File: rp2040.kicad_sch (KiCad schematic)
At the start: 27 parts, among them J3 Conn_01x02, J4 USB_B_Micro, U4 NCP1117-3.3_SOT223, U5 W25Q128JVS, U6 RP2040, Y2 ABM8-272-T3

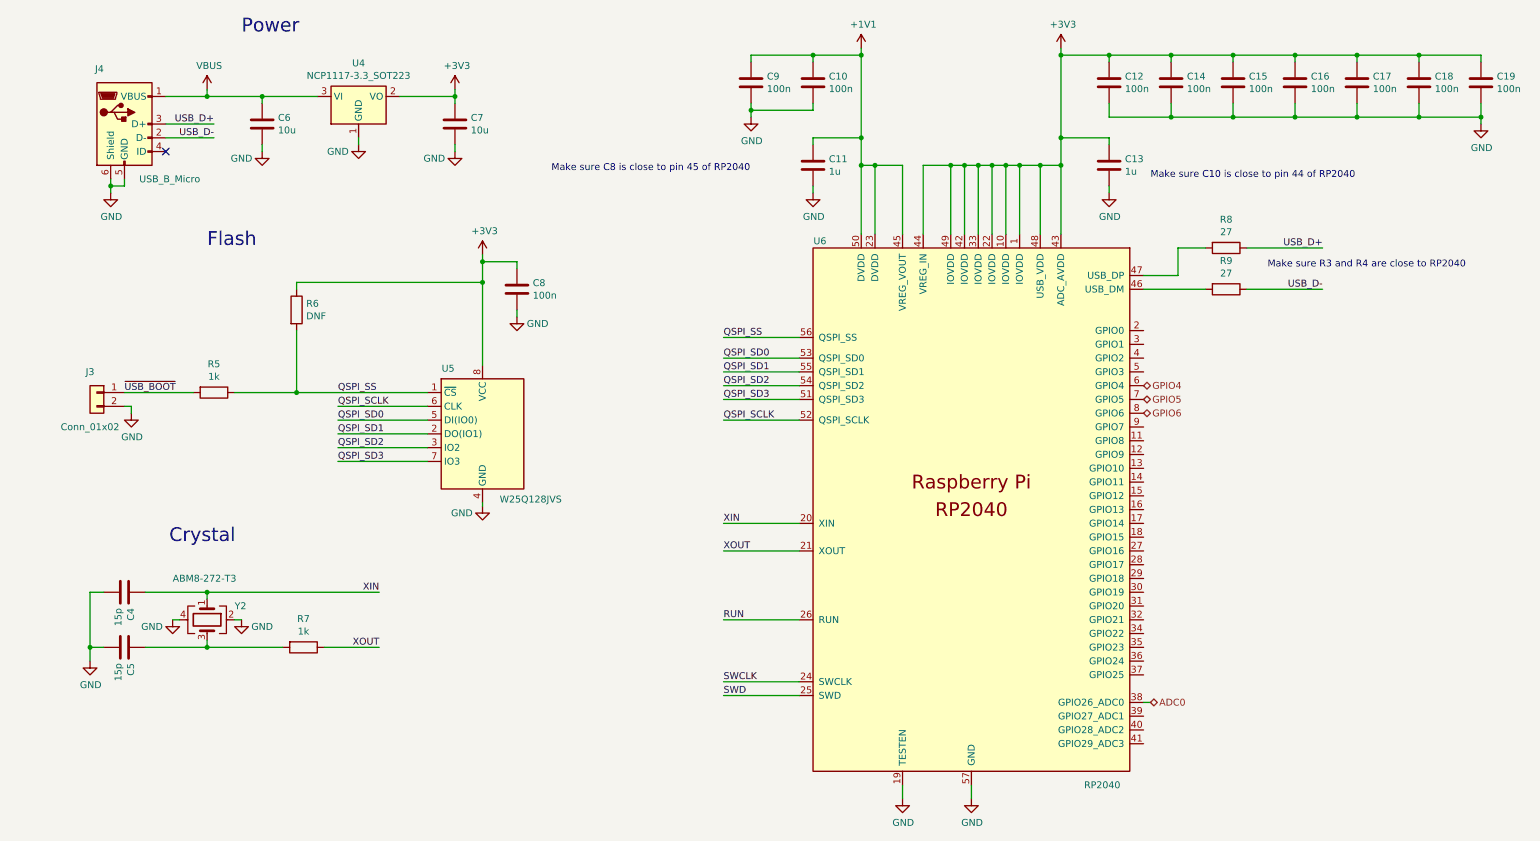
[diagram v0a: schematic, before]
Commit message: Finish most of the schematic design
The majority of the schematic is in a pretty finalized state now. Also
some more work on the PCB has been done.
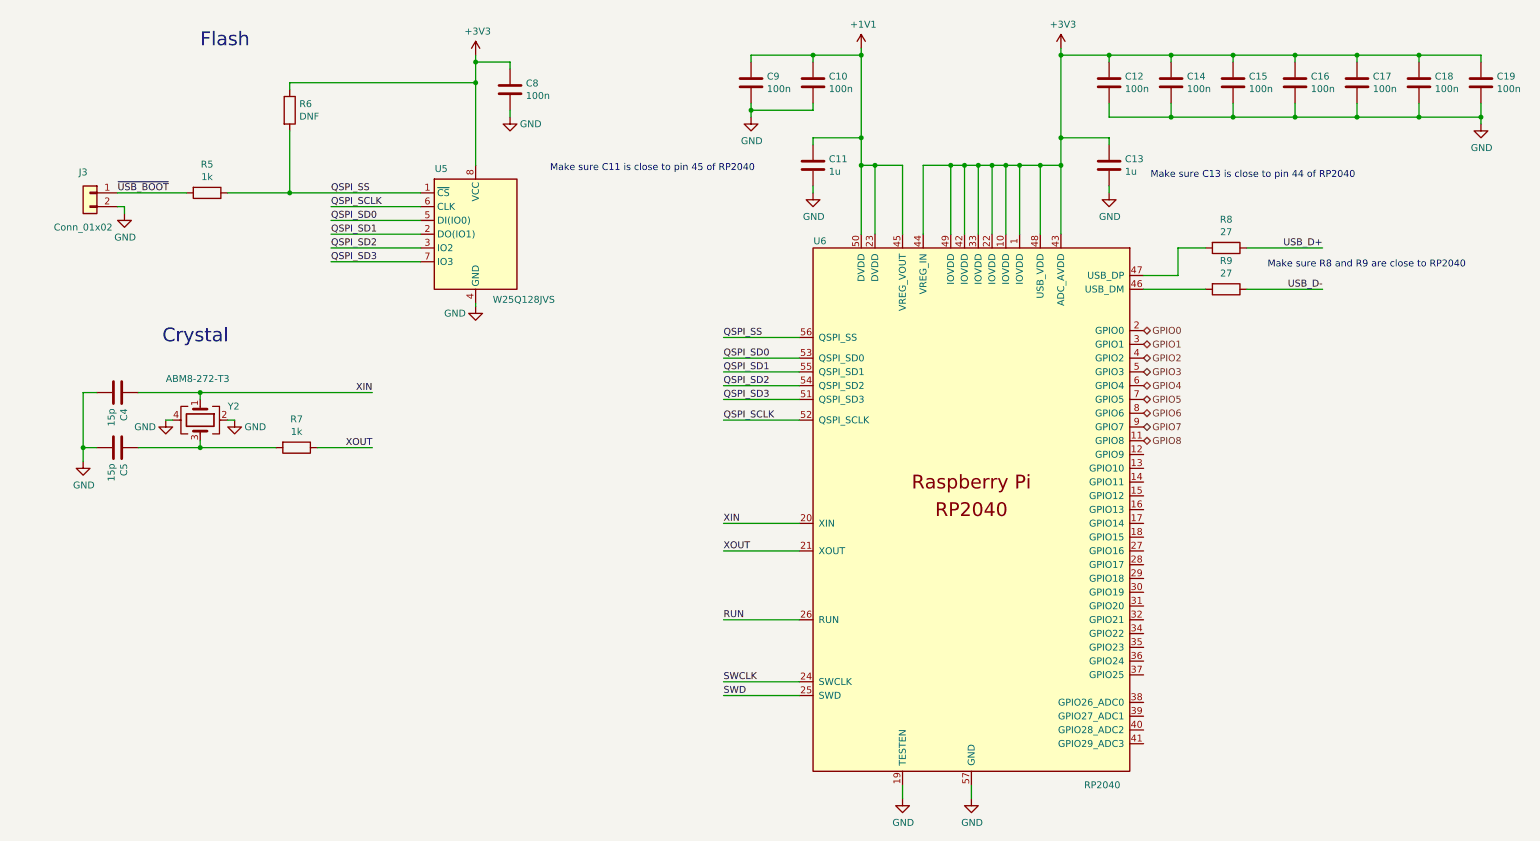
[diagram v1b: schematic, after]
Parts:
- removed C6, C7: 10u, Capacitor_SMD:C_0805_2012Metric, symbol Device:C
- removed J4: USB_B_Micro, RP2040_minimal:USB_Micro-B_Amphenol_10103594-0001LF_Horizontal_modified, symbol Connector:USB_B_Micro
- removed U4: NCP1117-3.3_SOT223, Package_TO_SOT_SMD:SOT-223-3_TabPin2, symbol Regulator_Linear:NCP1117-3.3_SOT223
- C10, C11, C12, C13, C14, C15, C16, C17, C18, C19, C4, C5, C8, C9: footprint Capacitor_SMD:C_0402_1005Metric -> Capacitor_SMD:C_0603_1608Metric
- R5, R6, R7, R8, R9: footprint Resistor_SMD:R_0402_1005Metric -> Resistor_SMD:R_0603_1608Metric
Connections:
- net GPIO8: now reaches U6.11 (GPIO8)
- net GPIO0: now reaches U6.2 (GPIO0)
- net GPIO1: now reaches U6.3 (GPIO1)
- net GPIO2: now reaches U6.4 (GPIO2)
- net GPIO3: now reaches U6.5 (GPIO3)
- net GPIO7: now reaches U6.9 (GPIO7)
- net ADC0: no longer names the net of U6.38 (GPIO26_ADC0)
- no-connect marks 1 -> 0
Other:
- note added: "Make sure C11 is close to pin 45 of RP2040"
- note added: "Make sure C13 is close to pin 44 of RP2040"
- note added: "Make sure R8 and R9 are close to RP2040"
- note removed: "Make sure C10 is close to pin 44 of RP2040"
- note removed: "Make sure C8 is close to pin 45 of RP2040"
- note removed: "Make sure R3 and R4 are close to RP2040"
- note removed: "Power"
- moved on the sheet: C4, C5, C8, J3, R5, R6, R7, U5, Y2

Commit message: Finish routing most of the PCB
The PCB should work now for the most part. Also fixes some miscellaneous
schematic things and swaps out a few components.
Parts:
- removed J3: Conn_01x02, Connector_PinHeader_2.54mm:PinHeader_1x02_P2.54mm_Vertical, symbol Connector_Generic:Conn_01x02
- added SW1: TS04-66-70-BK-160-SMT, TS04_66_70_BK_160_SMT2:SW_TS04-66-70-BK-160-SMT, symbol Switch:SW_Push
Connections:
- net GND: now also SW1.1
- net ~{USB_BOOT}: now also SW1.2
- net GPIO9: now reaches U6.12 (GPIO9)
- net GPIO26_ADC0: now reaches U6.38 (GPIO26_ADC0)
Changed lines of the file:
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@@
-	(wire
-		(pts
-			(xy 236.22 66.04) (xy 250.19 66.04)
-		)
-		(stroke
-			(width 0)
-			(type default)
-		)
-	)
 	(wire
 		(pts
@@
 	(wire
 		(pts
+			(xy 16.51 48.26) (xy 17.78 48.26)
+		)
+		(stroke
+			(width 0)
+			(type default)
+		)
+	)
+	(wire
+		(pts
 			(xy 233.68 24.13) (xy 233.68 22.86)
 		)
@@
 	(wire
 		(pts
+			(xy 237.49 66.04) (xy 236.22 66.04)
+		)
+		(stroke
+			(width 0)
+			(type default)
+		)
+	)
+	(wire
+		(pts
 			(xy 153.67 90.17) (xy 139.7 90.17)
 		)
@@
 	(wire
 		(pts
-			(xy 27.94 50.8) (xy 29.21 50.8)
-		)
-		(stroke
-			(width 0)
-			(type default)
-		)
-	)
-	(wire
-		(pts
 			(xy 194.31 43.18) (xy 194.31 55.88)
 		)
@@
 	(wire
 		(pts
-			(xy 29.21 50.8) (xy 29.21 52.07)
+			(xy 16.51 48.26) (xy 16.51 49.53)
 		)
 		(stroke
@@
 	(wire
 		(pts
-			(xy 236.22 58.42) (xy 250.19 58.42)
-		)
-		(stroke
-			(width 0)
-			(type default)
-		)
-	)
-	(wire
-		(pts
 			(xy 245.11 22.86) (xy 256.54 22.86)
 		)
@@
 		(pts
 			(xy 165.1 43.18) (xy 165.1 55.88)
+		)
+		(stroke
+			(width 0)
+			(type default)
+		)
+	)
+	(wire
+		(pts
+			(xy 237.49 58.42) (xy 236.22 58.42)
 		)
 		(stroke
@@
 		)
 	)
-	(label "USB_D+"
-		(at 250.19 58.42 180)
-		(effects
-			(font
-				(size 1.27 1.27)
-			)
-			(justify right bottom)
-		)
-	)
 	(label "XOUT"
 		(at 139.7 114.3 0)
@@
 			)
 			(justify left bottom)
-		)
-	)
-	(label "USB_D-"
-		(at 250.19 66.04 180)
-		(effects
-			(font
-				(size 1.27 1.27)
-			)
-			(justify right bottom)
 		)
 	)
@@
 		)
 	)
+	(hierarchical_label "USB_D-"
+		(shape bidirectional)
+		(at 237.49 66.04 0)
+		(effects
+			(font
+				(size 1.27 1.27)
+			)
+			(justify left)
+		)
+	)
 	(hierarchical_label "GPIO6"
 		(shape bidirectional)
@@
 		)
 	)
+	(hierarchical_label "USB_D+"
+		(shape bidirectional)
+		(at 237.49 58.42 0)
+		(effects
+			(font
+				(size 1.27 1.27)
+			)
+			(justify left)
+		)
+	)
 	(hierarchical_label "GPIO4"
 		(shape bidirectional)
 		(at 217.17 83.82 0)
+		(effects
+			(font
+				(size 1.27 1.27)
+			)
+			(justify left)
+		)
+	)
+	(hierarchical_label "GPIO9"
+		(shape bidirectional)
+		(at 217.17 96.52 0)
+		(effects
+			(font
+				(size 1.27 1.27)
+			)
+			(justify left)
+		)
+	)
+	(hierarchical_label "GPIO26_ADC0"
+		(shape bidirectional)
+		(at 217.17 142.24 0)
 		(effects
 			(font
@@
 	)
 	(symbol
+		(lib_id "Switch:SW_Push")
+		(at 22.86 48.26 0)
+		(unit 1)
+		(exclude_from_sim no)
+		(in_bom yes)
+		(on_board yes)
+		(dnp no)
+		(fields_autoplaced yes)
+		(property "Reference" "SW1"
+			(at 22.86 40.64 0)
+			(effects
+				(font
+					(size 1.27 1.27)
+				)
+			)
+		)
+		(property "Value" "TS04-66-70-BK-160-SMT"
+			(at 22.86 43.18 0)
+			(effects
+				(font
+					(size 1.27 1.27)
+				)
+			)
+		)
+		(property "Footprint" "TS04_66_70_BK_160_SMT2:SW_TS04-66-70-BK-160-SMT"
+			(at 22.86 43.18 0)
+			(effects
+				(font
+					(size 1.27 1.27)
+				)
+				(hide yes)
+			)
+		)
+		(property "Datasheet" "~"
+			(at 22.86 43.18 0)
+			(effects
+				(font
+					(size 1.27 1.27)
+				)
+				(hide yes)
+			)
+		)
+		(property "Description" "Push button switch, generic, two pins"
+			(at 22.86 48.26 0)
+			(effects
+				(font
+					(size 1.27 1.27)
+				)
+				(hide yes)
+			)
+		)
+		(pin "2"
+		)
+		(pin "1"
+		)
+		(instances
+			(project ""
+				(path "/bf621d61-5d08-4d1e-8172-14fa0e2cb1c4/13e9e744-a549-494b-a202-e1ef696ed4a6"
+					(reference "SW1")
+					(unit 1)
+				)
+			)
+		)
+	)
+	(symbol
 		(lib_id "power:GND")
-		(at 29.21 52.07 0)
+		(at 16.51 49.53 0)
 		(unit 1)
 		(exclude_from_sim no)
@@
 		(dnp no)
 		(property "Reference" "#PWR014"
-			(at 29.21 58.42 0)
+			(at 16.51 55.88 0)
 			(effects
 				(font
@@
 		)
 		(property "Value" "GND"
-			(at 29.337 56.4642 0)
+			(at 16.637 53.9242 0)
 			(effects
 				(font
@@
 		)
 		(property "Footprint" ""
-			(at 29.21 52.07 0)
+			(at 16.51 49.53 0)
 			(effects
 				(font
@@
 		)
 		(property "Datasheet" ""
-			(at 29.21 52.07 0)
+			(at 16.51 49.53 0)
 			(effects
 				(font
@@
 		)
 		(property "Description" ""
-			(at 29.21 52.07 0)
+			(at 16.51 49.53 0)
 			(effects
 				(font
@@
 					(unit 1)
 				)
-			)
-		)
-	)
-	(symbol
-		(lib_id "Connector_Generic:Conn_01x02")
-		(at 22.86 48.26 0)
-		(mirror y)
-		(unit 1)
-		(exclude_from_sim no)
-		(in_bom yes)
-		(on_board yes)
-		(dnp no)
-		(property "Reference" "J3"
-			(at 21.59 44.45 0)
-			(effects
-				(font
-					(size 1.27 1.27)
-				)
-			)
-		)
-		(property "Value" "Conn_01x02"
-			(at 21.59 54.61 0)
-			(effects
-				(font
-					(size 1.27 1.27)
-				)
-			)
-		)
-		(property "Footprint" "Connector_PinHeader_2.54mm:PinHeader_1x02_P2.54mm_Vertical"
-			(at 22.86 48.26 0)
-			(effects
-				(font
-					(size 1.27 1.27)
-				)
-				(hide yes)
-			)
-		)
-		(property "Datasheet" "~"
-			(at 22.86 48.26 0)
-			(effects
-				(font
-					(size 1.27 1.27)
-				)
-				(hide yes)
-			)
-		)
-		(property "Description" ""
-			(at 22.86 48.26 0)
-			(effects
-				(font
-					(size 1.27 1.27)
-				)
-			)
-		)
-		(pin "1"
-		)
-		(pin "2"
-		)
-		(instances
-			(project "Motorized Fader Driver"
-				(path "/bf621d61-5d08-4d1e-8172-14fa0e2cb1c4/13e9e744-a549-494b-a202-e1ef696ed4a6"
-					(reference "J3")
-					(unit 1)
-				)

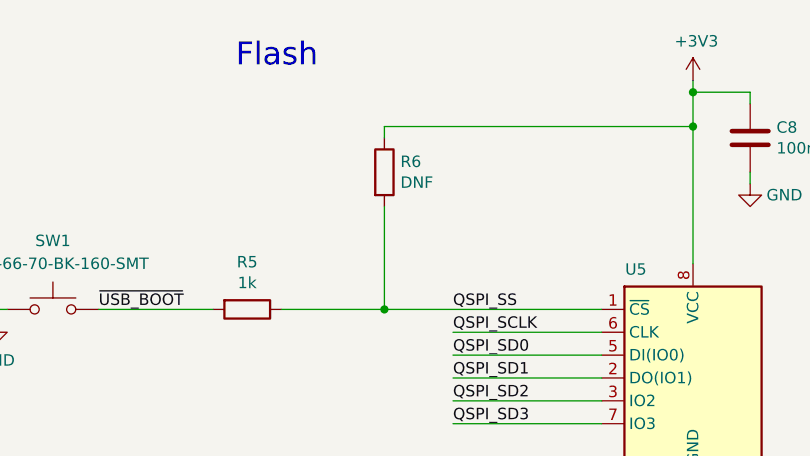
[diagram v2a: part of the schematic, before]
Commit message: Route more things and add LCSC part numbers for things
The LCSC part numbers allow for JLCPCB's PCBA tool to find the parts.
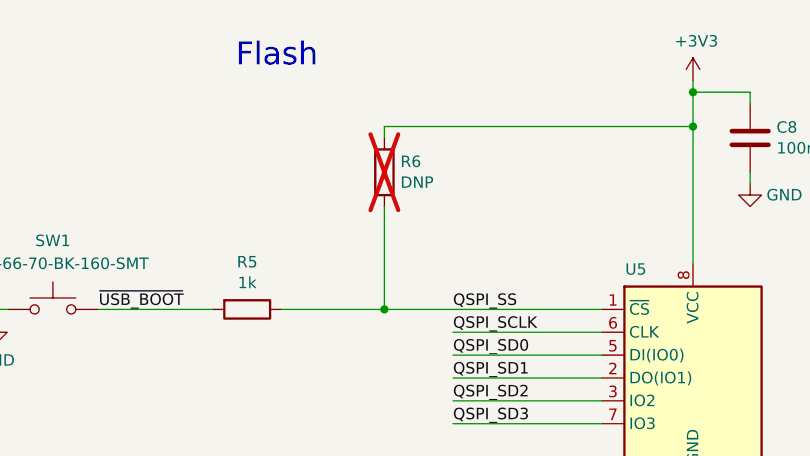
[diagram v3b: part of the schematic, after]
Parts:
- C10, C12, C14, C15, C16, C17, C18, C19, C8, C9: LCSC Part (none) -> C76711
- C11, C13: LCSC Part (none) -> C76706
- C4, C5: LCSC Part (none) -> C342889
- R5, R7: LCSC Part (none) -> C21190
- R6: value DNF -> DNP; now not fitted
- R8, R9: LCSC Part (none) -> C2907021
- SW1: LCSC Part (none) -> C4364350
- U5: LCSC Part (none) -> C97521
- U6: LCSC Part (none) -> C2040
- Y2: LCSC Part (none) -> C20625731
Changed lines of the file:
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@@
+			)
+		)
+		(property "LCSC Part" "C76711"
+			(at 156.21 27.94 0)
+			(effects
+				(font
+					(size 1.27 1.27)
+				)
+				(hide yes)
 			)
 		)
@@
 			)
 		)
+		(property "LCSC Part" "C21190"
+			(at 60.96 95.25 0)
+			(effects
+				(font
+					(size 1.27 1.27)
+				)
+				(hide yes)
+			)
+		)
 		(pin "1"
 		)
@@
 			)
 		)
+		(property "LCSC Part" "C76711"
+			(at 279.4 27.94 0)
+			(effects
+				(font
+					(size 1.27 1.27)
+				)
+				(hide yes)
+			)
+		)
 		(pin "1"
 		)
@@
 			)
 		)
+		(property "LCSC Part" "C342889"
+			(at 27.94 95.25 0)
+			(effects
+				(font
+					(size 1.27 1.27)
+				)
+				(hide yes)
+			)
+		)
 		(pin "1"
 		)
@@
 			)
 		)
+		(property "LCSC Part" "C76706"
+			(at 210.82 43.18 0)
+			(effects
+				(font
+					(size 1.27 1.27)
+				)
+				(hide yes)
+			)
+		)
 		(pin "1"
 		)
@@
 			)
 		)
+		(property "LCSC Part" "C76711"
+			(at 245.11 27.94 0)
+			(effects
+				(font
+					(size 1.27 1.27)
+				)
+				(hide yes)
+			)
+		)
 		(pin "1"
 		)
@@
 			)
 		)
+		(property "LCSC Part" "C97521"
+			(at 93.98 55.88 0)
+			(effects
+				(font
+					(size 1.27 1.27)
+				)
+				(hide yes)
+			)
+		)
 		(pin "1"
 		)
@@
 			)
 		)
+		(property "LCSC Part" "C76711"
+			(at 222.25 27.94 0)
+			(effects
+				(font
+					(size 1.27 1.27)
+				)
+				(hide yes)
+			)
+		)
 		(pin "1"
 		)
@@
 			)
 		)
+		(property "LCSC Part" "C76711"
+			(at 210.82 27.94 0)
+			(effects
+				(font
+					(size 1.27 1.27)
+				)
+				(hide yes)
+			)
+		)
 		(pin "1"
 		)
@@
 			)
 		)
+		(property "LCSC Part" "C21190"
+			(at 44.45 48.26 0)
+			(effects
+				(font
+					(size 1.27 1.27)
+				)
+				(hide yes)
+			)
+		)
 		(pin "1"
 		)
@@
 			)
 		)
+		(property "LCSC Part" "C2907021"
+			(at 232.41 58.42 0)
+			(effects
+				(font
+					(size 1.27 1.27)
+				)
+				(hide yes)
+			)
+		)
 		(pin "1"
 		)
@@
 			)
 		)
+		(property "LCSC Part" "C76706"
+			(at 156.21 43.18 0)
+			(effects
+				(font
+					(size 1.27 1.27)
+				)
+				(hide yes)
+			)
+		)
 		(pin "1"
 		)
@@
 			)
 		)
+		(property "LCSC Part" "C342889"
+			(at 27.94 85.09 0)
+			(effects
+				(font
+					(size 1.27 1.27)
+				)
+				(hide yes)
+			)
+		)
 		(pin "1"
 		)
@@
 					(size 1.27 1.27)
 				)
+			)
+		)
+		(property "LCSC Part" "C76711"
+			(at 100.33 29.21 0)
+			(effects
+				(font
+					(size 1.27 1.27)
+				)
+				(hide yes)
 			)
 		)
@@
 			)
 		)
+		(property "LCSC Part" "C4364350"
+			(at 22.86 48.26 0)
+			(effects
+				(font
+					(size 1.27 1.27)
+				)
+				(hide yes)
+			)
+		)
 		(pin "2"
 		)
@@
 			)
 		)
+		(property "LCSC Part" "C20625731"
+			(at 43.18 90.17 0)
+			(effects
+				(font
+					(size 1.27 1.27)
+				)
+				(hide yes)
+			)
+		)
 		(pin "1"
 		)
@@
 			)
 		)
+		(property "LCSC Part" "C2907021"
+			(at 232.41 66.04 0)
+			(effects
+				(font
+					(size 1.27 1.27)
+				)
+				(hide yes)
+			)
+		)
 		(pin "1"
 		)
@@
 			)
 		)
+		(property "LCSC Part" "C2040"
+			(at 185.42 106.68 0)
+			(effects
+				(font
+					(size 1.27 1.27)
+				)
+				(hide yes)
+			)
+		)
 		(pin "1"
 		)
@@
 			)
 		)
+		(property "LCSC Part" "C76711"
+			(at 256.54 27.94 0)
+			(effects
+				(font
+					(size 1.27 1.27)
+				)
+				(hide yes)
+			)
+		)
 		(pin "1"
 		)
@@
 			)
 		)
+		(property "LCSC Part" "C76711"
+			(at 233.68 27.94 0)
+			(effects
+				(font
+					(size 1.27 1.27)
+				)
+				(hide yes)
+			)
+		)
 		(pin "1"
 		)
@@
 			)
 		)
+		(property "LCSC Part" "C76711"
+			(at 144.78 27.94 0)
+			(effects
+				(font
+					(size 1.27 1.27)
+				)
+				(hide yes)
+			)
+		)
 		(pin "1"
 		)
@@
 			)
 		)
+		(property "LCSC Part" "C76711"
+			(at 267.97 27.94 0)
+			(effects
+				(font
+					(size 1.27 1.27)
+				)
+				(hide yes)
+			)
+		)
 		(pin "1"
 		)
@@
 		(in_bom yes)
 		(on_board yes)
-		(dnp no)
+		(dnp yes)
 		(property "Reference" "R6"
 			(at 61.468 31.8516 0)
@@
 			)
 		)
-		(property "Value" "DNF"
+		(property "Value" "DNP"
 			(at 61.468 34.163 0)
 			(effects
